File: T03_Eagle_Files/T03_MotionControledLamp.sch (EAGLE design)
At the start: 32 parts, among them SW1 RESET, U1 ATMEGA328P-MU, U2 V_REG_LD1085D2, U4 TPS61161ADRVT, X2 16MHz

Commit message: Implementing Feedback
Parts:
- removed R2: 10K, Smartprj:R-EU_R0603
- removed U$11: DISCLAIMER, Smartprj:DISCLAIMER
- removed U2: V_REG_LD1085D2, SparkFun-PowerIC:V_REG_LD1085D2
- added IC1: L7805, v-reg:78XXL
- added JP2: BAT_POS_VOLT, adafruit:PINHD-1X1
- added JP3: BAT_GND, adafruit:PINHD-1X1
- added R3: 10k, rcl:R-US_M1206
- C5: value 100uF -> 10uF
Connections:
- net IO10 renamed PWM_LEDS
- net IO11 renamed MOSI
- net IO12 renamed MISO
- removed net ADC0: U1.PC0(ADC0)
- removed net ADC1: U1.PC1(ADC1)
- removed net ADC2: U1.PC2(ADC2)
- removed net ADC3: U1.PC3(ADC3)
- removed net ADC4: U1.PC4(ADC4/SDA)
- removed net ADC5: U1.PC5(ADC5/SCL)
- removed net ADC6: U1.ADC6
- removed net ADC7: U1.ADC7
- removed net IO2: U1.PD2(INT0)
- removed net IO3: U1.PD3(INT1)
- removed net IO4: U1.PD4(XCK/T0)
- removed net IO5: U1.PD5(T1)
- removed net IO6: U1.PD6(AIN0)
- removed net IO7: U1.PD7(AIN1)
- removed net IO8: U1.PB0(ICP)
- removed net IO9: U1.PB1(OC1A)
- removed net N$5: JP1.7, U1.PB5(SCK)
- removed net VCC: PWR_SWTCH.P
- new net +V_BAT: JP2.1, PWR_SWTCH.P
- new net NC: U1.ADC6, U1.ADC7, U1.PB0(ICP), U1.PB1(OC1A), U1.PC0(ADC0), U1.PC1(ADC1), U1.PC2(ADC2), U1.PC3(ADC3), U1.PC4(ADC4/SDA), U1.PC5(ADC5/SCL), U1.PD2(INT0), U1.PD3(INT1), U1.PD4(XCK/T0), U1.PD5(T1), U1.PD6(AIN0), U1.PD7(AIN1)
- net +5V: now also IC1.OUT, R3.2; no longer R2.2, U2.OUT, U2.OUT@1
- net GND: now also IC1.GND, JP1.4, JP3.1; no longer U2.ADJ
- net N$4: now also IC1.IN; no longer U2.IN
- net RST: now also JP1.7, R3.1, U1.PB5(SCK); no longer R2.1
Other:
- note added: "1W Natural White LED"
- note added: "350 mA 3.2-3.6 V drop"
- note added: "BREAK UP THESE CONNECTIONS!"
- note added: "LED DRIVER 38V max 700mA"
- note added: "Move LEDs off of board onto their own PCB"
- note added: "Team 3"
- note added: "Using original Arduino Schematic for 328p usage."
- note removed: "AVR ISP Programmer Header"
- note removed: "LM1085 5V 3A OUT"
- note removed: "LM1085 WHY TWO OUT?"
- moved on the sheet: C6, C8, C9, D1, L1, LED1, LED2, LED3, LED4, LED5, LED6, LED7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

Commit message: Breakout Board Schematics + Layout
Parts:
- removed LED1, LED2, LED3, LED4, LED5, LED6, LED7, LED8: LAW57B, led:LAW57B
- removed U$3: ULTRASONIC-HC-SR04, diy-modules:ULTRASONIC-HC-SR04
- added JP4: LED_V+, adafruit:PINHD-1X1
- added JP5: LED_V-, adafruit:PINHD-1X1
- added SR04: 22-23-2041, con-molex:22-23-2041
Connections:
- removed net N$10: LED3.C, LED5.A
- removed net N$11: LED5.C, LED8.A
- removed net N$12: LED3.A, LED6.C
- removed net N$15: LED4.C, LED7.A
- removed net N$7: LED1.C, LED2.A
- removed net N$8: LED2.C, LED4.A
- removed net N$9: LED6.A, LED7.C
- net +5V: now also SR04-1.S; no longer U$3.VCC
- net GND: now also SR04-4.S; no longer U$3.GND
- net MISO: now also SR04-2.S; no longer U$3.TRIG
- net MOSI: now also SR04-3.S; no longer U$3.ECHO
- net N$14: now also JP5.1; no longer LED8.C
- net N$6: no longer LED1.A
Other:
- note added: "ECHO"
- note added: "GND"
- note added: "TRIG"
- note added: "VCC"
- note removed: "Move LEDs off of board onto their own PCB"

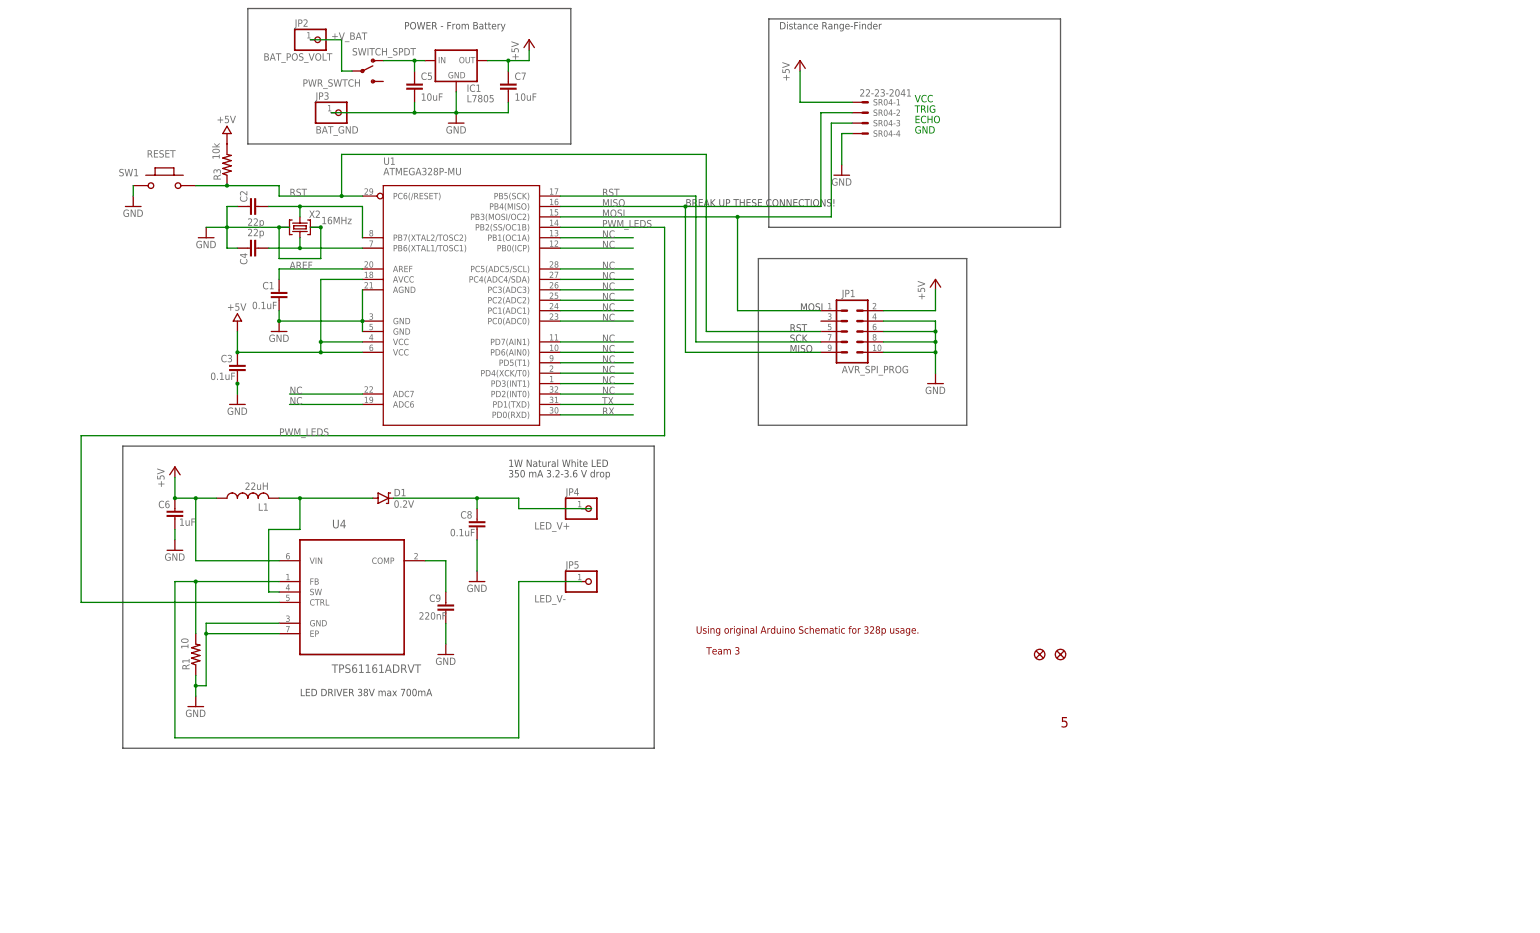
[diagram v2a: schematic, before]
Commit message: Started routing. Has polygon ready. Just ratsnest and then name the polygon to GND
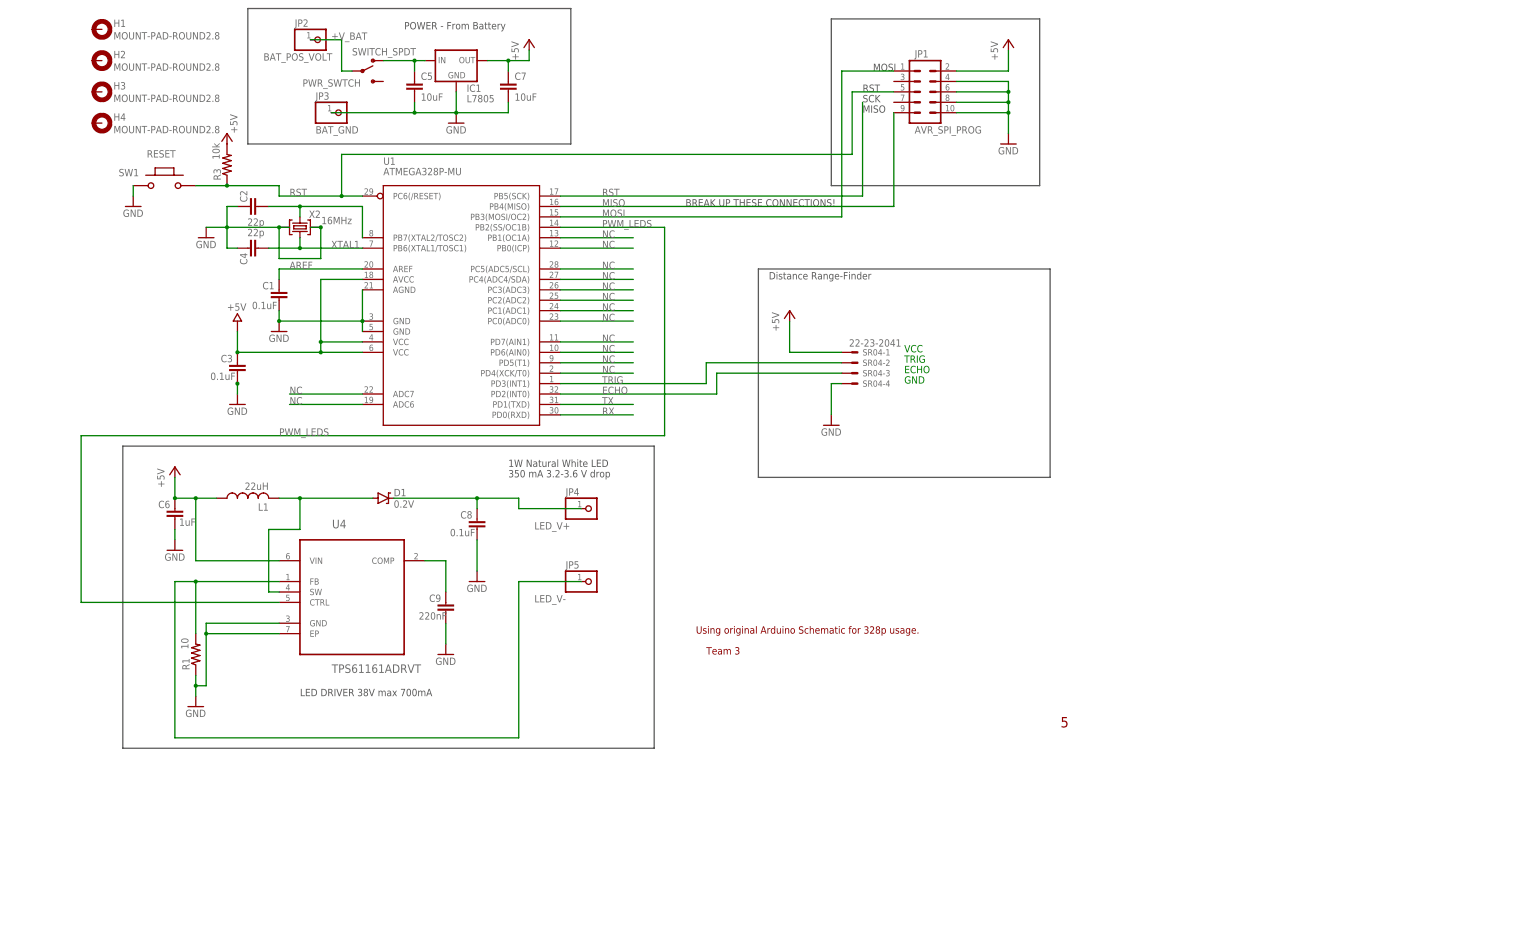
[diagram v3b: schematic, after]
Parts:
- removed U$2, U$4: FIDUCIAL1X2, SparkFun:FIDUCIAL1X2
- added H1, H2, H3, H4: MOUNT-PAD-ROUND2.8, holes:MOUNT-PAD-ROUND2.8
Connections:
- net N$1 renamed XTAL1
- net N$2 renamed XTAL2
- new net ECHO: SR04-3.S, U1.PD2(INT0)
- new net TRIG: SR04-2.S, U1.PD3(INT1)
- net MISO: no longer SR04-2.S
- net MOSI: no longer SR04-3.S
- net N$6: now also JP4.1
- net NC: no longer U1.PD2(INT0), U1.PD3(INT1)
- net RST: no longer JP1.7
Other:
- moved on the sheet: JP1, SR04-1, SR04-2, SR04-3, SR04-4

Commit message: Completed Board Layout First Draft
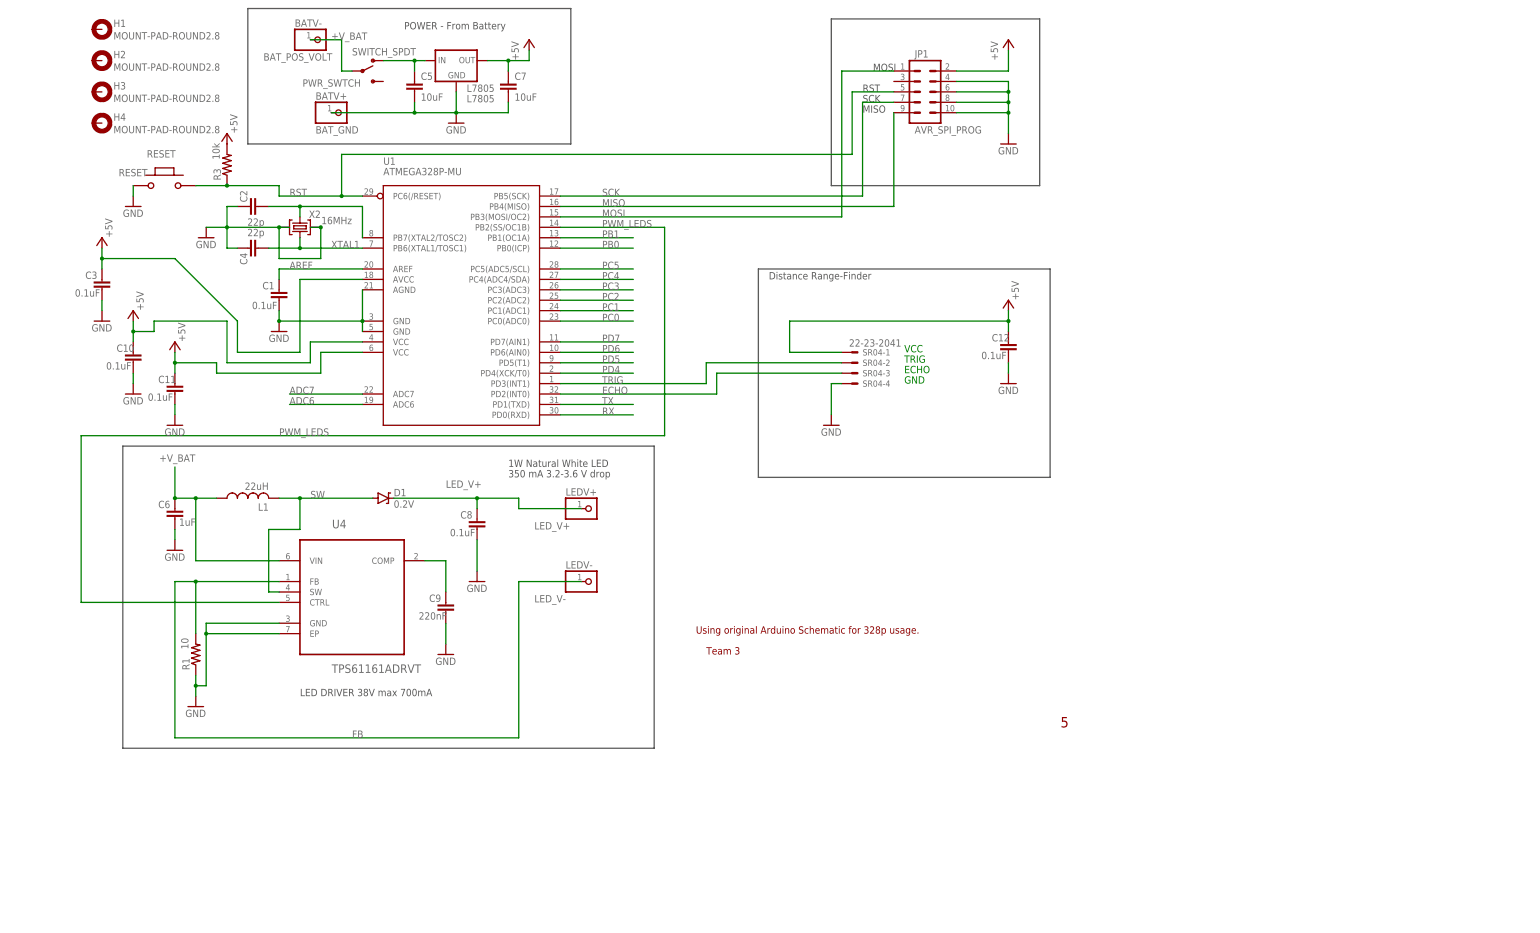
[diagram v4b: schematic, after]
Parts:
- added C10, C11, C12: 0.1uF, Smartprj:C-EUC0603
- U1: device Smartprj:ATMEGAXX8-MU -> Smartprj:ATMEGAXX8-AU
- renumbered IC1 to L7805, JP2 to BATV-, JP3 to BATV+, JP4 to LEDV+, JP5 to LEDV-, SW1 to RESET
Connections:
- net N$13 renamed COMP
- net N$14 renamed FB
- net N$3 renamed SW
- net N$6 renamed LED_V+
- removed net NC: U1.ADC6, U1.ADC7, U1.PB0(ICP), U1.PB1(OC1A), U1.PC0(ADC0), U1.PC1(ADC1), U1.PC2(ADC2), U1.PC3(ADC3), U1.PC4(ADC4/SDA), U1.PC5(ADC5/SCL), U1.PD4(XCK/T0), U1.PD5(T1), U1.PD6(AIN0), U1.PD7(AIN1)
- new net ADC6: U1.ADC6
- new net ADC7: U1.ADC7
- new net PB0: U1.PB0(ICP)
- new net PB1: U1.PB1(OC1A)
- new net PC0: U1.PC0(ADC0)
- new net PC1: U1.PC1(ADC1)
- new net PC2: U1.PC2(ADC2)
- new net PC3: U1.PC3(ADC3)
- new net PC4: U1.PC4(ADC4/SDA)
- new net PC5: U1.PC5(ADC5/SCL)
- new net PD4: U1.PD4(XCK/T0)
- new net PD5: U1.PD5(T1)
- new net PD6: U1.PD6(AIN0)
- new net PD7: U1.PD7(AIN1)
- new net SCK: JP1.7, U1.PB5(SCK)
- net +5V: now also C10.2, C11.2, C12.2; no longer C6.2, L1.1, U4.VIN
- net +V_BAT: now also C6.2, L1.1, U4.VIN
- net GND: now also C10.1, C11.1, C12.1
- net RST: no longer U1.PB5(SCK)
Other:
- note removed: "BREAK UP THESE CONNECTIONS!"
- moved on the sheet: C3

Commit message: Updated values of components and symbols for Board Layout
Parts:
- BATV+: value BAT_GND -> BAT_POS_VOLT
- BATV-: value BAT_POS_VOLT -> BAT_GND
- C8: value 0.1uF -> 10uF
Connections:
- net +V_BAT: now also BATV+.1; no longer BATV-.1
- net GND: now also BATV-.1; no longer BATV+.1
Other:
- moved on the sheet: BATV+, BATV-
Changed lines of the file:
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@@
 <part name="L1" library="rcl" deviceset="L-US" device="L4532P" value="22uH"/>
 <part name="C6" library="Smartprj" deviceset="C-EU" device="C0603" value="1uF"/>
-<part name="C8" library="Smartprj" deviceset="C-EU" device="C0603" value="0.1uF"/>
+<part name="C8" library="Smartprj" deviceset="C-EU" device="C0603" value="10uF"/>
 <part name="C9" library="Smartprj" deviceset="C-EU" device="C0603" value="220nF"/>
 <part name="R1" library="rcl" deviceset="R-US_" device="M1206" value="10"/>
@@
 <part name="GND10" library="supply1" deviceset="GND" device=""/>
 <part name="GND11" library="supply1" deviceset="GND" device=""/>
-<part name="BATV-" library="adafruit" deviceset="PINHD-1X1" device="" value="BAT_POS_VOLT"/>
-<part name="BATV+" library="adafruit" deviceset="PINHD-1X1" device="" value="BAT_GND"/>
+<part name="BATV+" library="adafruit" deviceset="PINHD-1X1" device="" value="BAT_POS_VOLT"/>
+<part name="BATV-" library="adafruit" deviceset="PINHD-1X1" device="" value="BAT_GND"/>
 <part name="R3" library="rcl" deviceset="R-US_" device="M1206" value="10k"/>
 <part name="L7805" library="v-reg" deviceset="78XXL" device="" value="L7805"/>
@@
 <instance part="GND10" gate="1" x="25.4" y="50.8"/>
 <instance part="GND11" gate="1" x="91.44" y="25.4"/>
-<instance part="BATV-" gate="G$1" x="60.96" y="175.26" smashed="yes">
+<instance part="BATV+" gate="G$1" x="60.96" y="175.26" smashed="yes">
 <attribute name="NAME" x="54.61" y="178.435" size="1.778" layer="95"/>
 <attribute name="VALUE" x="46.99" y="170.18" size="1.778" layer="96"/>
 </instance>
-<instance part="BATV+" gate="G$1" x="66.04" y="157.48" smashed="yes">
+<instance part="BATV-" gate="G$1" x="66.04" y="157.48" smashed="yes">
 <attribute name="NAME" x="59.69" y="160.655" size="1.778" layer="95"/>
 <attribute name="VALUE" x="59.69" y="152.4" size="1.778" layer="96"/>
@@
 <wire x1="83.82" y1="157.48" x2="93.98" y2="157.48" width="0.1524" layer="91"/>
 <junction x="83.82" y="157.48"/>
-<pinref part="BATV+" gate="G$1" pin="1"/>
+<pinref part="BATV-" gate="G$1" pin="1"/>
 <wire x1="83.82" y1="157.48" x2="63.5" y2="157.48" width="0.1524" layer="91"/>
 <pinref part="L7805" gate="A" pin="GND"/>
@@
 <pinref part="PWR_SWTCH" gate="G$1" pin="P"/>
 <wire x1="66.04" y1="167.64" x2="68.58" y2="167.64" width="0.1524" layer="91"/>
-<pinref part="BATV-" gate="G$1" pin="1"/>
+<pinref part="BATV+" gate="G$1" pin="1"/>
 <wire x1="66.04" y1="175.26" x2="58.42" y2="175.26" width="0.1524" layer="91"/>
 <label x="63.5" y="175.26" size="1.778" layer="95"/>
